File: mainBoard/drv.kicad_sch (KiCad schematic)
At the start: 6 parts

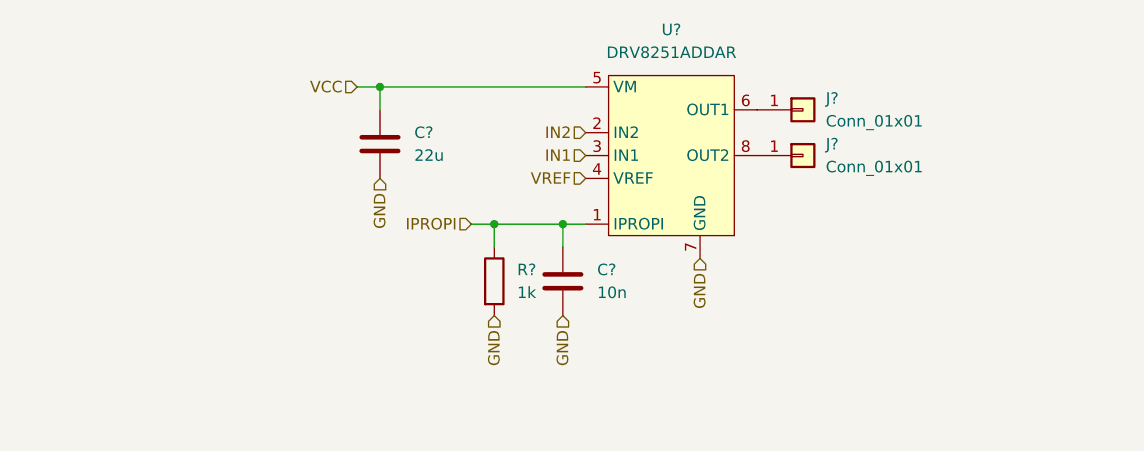
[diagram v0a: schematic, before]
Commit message: LEDky, měření napájení, připojení DRV atd.
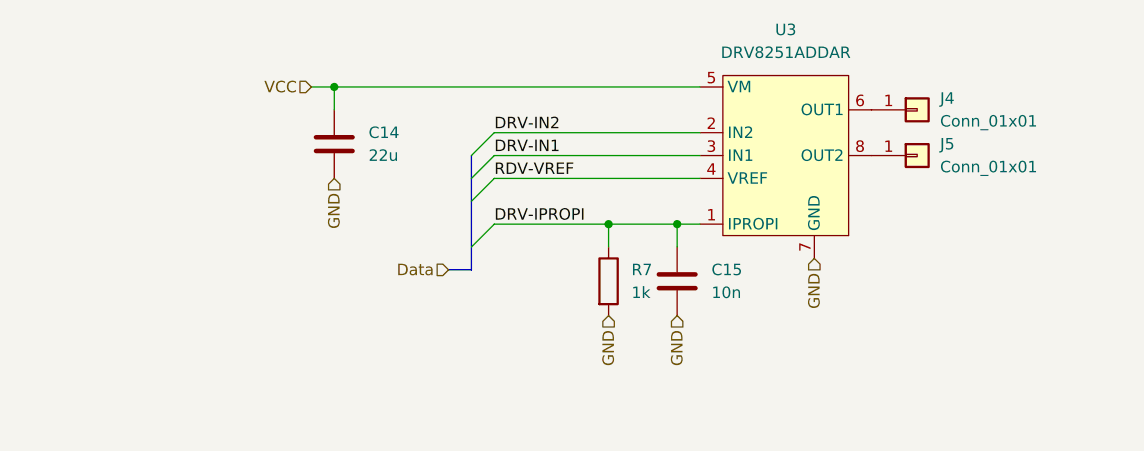
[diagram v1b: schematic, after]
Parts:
- gave numbers to parts that had none: 6
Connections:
- net IN1 renamed DRV-IN1
- net IN2 renamed DRV-IN2
- net IPROPI renamed DRV-IPROPI
- net VREF renamed RDV-VREF
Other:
- moved on the sheet: C14, C15, J4, J5, R7, U3

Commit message: Pouzdra
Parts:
- J4, J5: footprint (none) -> Connector_Pin:Pin_D1.0mm_L10.0mm
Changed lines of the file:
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@@
       (effects (font (size 1.27 1.27)) (justify left))
     )
-    (property "Footprint" "" (at 179.07 78.74 0)
+    (property "Footprint" "Connector_Pin:Pin_D1.0mm_L10.0mm" (at 179.07 78.74 0)
       (effects (font (size 1.27 1.27)) hide)
     )
@@
       (effects (font (size 1.27 1.27)) (justify left))
     )
-    (property "Footprint" "" (at 179.07 83.82 0)
+    (property "Footprint" "Connector_Pin:Pin_D1.0mm_L10.0mm" (at 179.07 83.82 0)
       (effects (font (size 1.27 1.27)) hide)
     )

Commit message: test-pointy a zdvojení konektorů
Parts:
- added J8: Conn_01x02, Connector_Phoenix_MC:PhoenixContact_MCV_1,5_2-G-3.81_1x02_P3.81mm_Vertical, symbol Connector_Generic:Conn_01x02
- added TP1, TP2: Conn_01x01, Connector_Pin:Pin_D0.7mm_L6.5mm_W1.8mm_FlatFork, symbol Connector_Generic:Conn_01x01
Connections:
- net DRV-IPROPI: now also TP1.1 (Pin_1)
- net RDV-VREF: now also TP2.1 (Pin_1)
- net at J4.1 (Pin_1), U3.6 (OUT1): now also J8.2 (Pin_2)
- net at J5.1 (Pin_1), U3.8 (OUT2): now also J8.1 (Pin_1)
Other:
- moved on the sheet: C14, J4, J5

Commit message: WIP
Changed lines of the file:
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@@
   (junction (at 152.4 91.44) (diameter 0) (color 0 0 0 0)
   )
-  (bus_entry (at 114.3 88.9) (size 2.54 -2.54)
-    (stroke (width 0) (type default))
-  )
-  (bus_entry (at 114.3 86.36) (size 2.54 -2.54)
-    (stroke (width 0) (type default))
-  )
-  (bus_entry (at 114.3 93.98) (size 2.54 -2.54)
-    (stroke (width 0) (type default))
-  )
-  (bus_entry (at 114.3 83.82) (size 2.54 -2.54)
+  (bus_entry (at 116.84 86.36) (size -2.54 2.54)
+    (stroke (width 0) (type default))
+  )
+  (bus_entry (at 116.84 83.82) (size -2.54 2.54)
+    (stroke (width 0) (type default))
+  )
+  (bus_entry (at 116.84 81.28) (size -2.54 2.54)
+    (stroke (width 0) (type default))
+  )
+  (bus_entry (at 116.84 91.44) (size -2.54 2.54)
     (stroke (width 0) (type default))
   )
@@
     (stroke (width 0) (type default))
   )
+  (wire (pts (xy 144.78 91.44) (xy 144.78 93.98))
+    (stroke (width 0) (type default))
+  )
+  (wire (pts (xy 96.52 76.2) (xy 99.06 76.2))
+    (stroke (width 0) (type default))
+  )
+  (wire (pts (xy 139.7 91.44) (xy 144.78 91.44))
+    (stroke (width 0) (type default))
+  )
+  (wire (pts (xy 176.53 78.74) (xy 173.99 78.74))
+    (stroke (width 0) (type default))
+  )
+  (wire (pts (xy 179.07 88.9) (xy 179.07 83.82))
+    (stroke (width 0) (type default))
+  )
+  (wire (pts (xy 152.4 91.44) (xy 154.94 91.44))
+    (stroke (width 0) (type default))
+  )
+  (wire (pts (xy 132.08 86.36) (xy 132.08 93.98))
+    (stroke (width 0) (type default))
+  )
+  (wire (pts (xy 181.61 83.82) (xy 179.07 83.82))
+    (stroke (width 0) (type default))
+  )
+  (wire (pts (xy 116.84 91.44) (xy 139.7 91.44))
+    (stroke (width 0) (type default))
+  )
+  (wire (pts (xy 181.61 88.9) (xy 179.07 88.9))
+    (stroke (width 0) (type default))
+  )
+  (wire (pts (xy 116.84 81.28) (xy 154.94 81.28))
+    (stroke (width 0) (type default))
+  )
+  (bus (pts (xy 111.76 96.52) (xy 114.3 96.52))
+    (stroke (width 0) (type default))
+  )
+  (wire (pts (xy 152.4 91.44) (xy 152.4 93.98))
+    (stroke (width 0) (type default))
+  )
+  (wire (pts (xy 116.84 83.82) (xy 154.94 83.82))
+    (stroke (width 0) (type default))
+  )
   (bus (pts (xy 114.3 83.82) (xy 114.3 86.36))
     (stroke (width 0) (type default))
   )
-  (wire (pts (xy 144.78 91.44) (xy 144.78 93.98))
-    (stroke (width 0) (type default))
-  )
-  (wire (pts (xy 96.52 76.2) (xy 99.06 76.2))
-    (stroke (width 0) (type default))
-  )
-  (wire (pts (xy 139.7 91.44) (xy 144.78 91.44))
-    (stroke (width 0) (type default))
-  )
-  (wire (pts (xy 176.53 78.74) (xy 173.99 78.74))
-    (stroke (width 0) (type default))
-  )
-  (wire (pts (xy 179.07 88.9) (xy 179.07 83.82))
-    (stroke (width 0) (type default))
-  )
-  (wire (pts (xy 152.4 91.44) (xy 154.94 91.44))
-    (stroke (width 0) (type default))
-  )
-  (wire (pts (xy 132.08 86.36) (xy 132.08 93.98))
-    (stroke (width 0) (type default))
-  )
-  (wire (pts (xy 181.61 83.82) (xy 179.07 83.82))
-    (stroke (width 0) (type default))
-  )
-  (wire (pts (xy 116.84 91.44) (xy 139.7 91.44))
-    (stroke (width 0) (type default))
-  )
-  (wire (pts (xy 181.61 88.9) (xy 179.07 88.9))
-    (stroke (width 0) (type default))
-  )
-  (wire (pts (xy 116.84 81.28) (xy 154.94 81.28))
+  (wire (pts (xy 179.07 83.82) (xy 173.99 83.82))
     (stroke (width 0) (type default))
   )
@@
     (stroke (width 0) (type default))
   )
-  (bus (pts (xy 111.76 96.52) (xy 114.3 96.52))
-    (stroke (width 0) (type default))
-  )
-  (wire (pts (xy 152.4 91.44) (xy 152.4 93.98))
-    (stroke (width 0) (type default))
-  )
-  (wire (pts (xy 116.84 83.82) (xy 154.94 83.82))
+  (wire (pts (xy 132.08 86.36) (xy 154.94 86.36))
+    (stroke (width 0) (type default))
+  )
+  (wire (pts (xy 116.84 86.36) (xy 132.08 86.36))
+    (stroke (width 0) (type default))
+  )
+  (wire (pts (xy 181.61 78.74) (xy 176.53 78.74))
+    (stroke (width 0) (type default))
+  )
+  (wire (pts (xy 176.53 91.44) (xy 176.53 78.74))
+    (stroke (width 0) (type default))
+  )
+  (wire (pts (xy 181.61 91.44) (xy 176.53 91.44))
+    (stroke (width 0) (type default))
+  )
+  (wire (pts (xy 99.06 76.2) (xy 99.06 78.74))
+    (stroke (width 0) (type default))
+  )
+  (wire (pts (xy 144.78 91.44) (xy 152.4 91.44))
     (stroke (width 0) (type default))
   )
   (bus (pts (xy 114.3 86.36) (xy 114.3 88.9))
-    (stroke (width 0) (type default))
-  )
-  (wire (pts (xy 179.07 83.82) (xy 173.99 83.82))
-    (stroke (width 0) (type default))
-  )
-  (wire (pts (xy 132.08 86.36) (xy 154.94 86.36))
-    (stroke (width 0) (type default))
-  )
-  (wire (pts (xy 181.61 78.74) (xy 176.53 78.74))
-    (stroke (width 0) (type default))
-  )
-  (wire (pts (xy 176.53 91.44) (xy 176.53 78.74))
-    (stroke (width 0) (type default))
-  )
-  (wire (pts (xy 181.61 91.44) (xy 176.53 91.44))
-    (stroke (width 0) (type default))
-  )
-  (wire (pts (xy 116.84 86.36) (xy 132.08 86.36))
-    (stroke (width 0) (type default))
-  )
-  (wire (pts (xy 99.06 76.2) (xy 99.06 78.74))
-    (stroke (width 0) (type default))
-  )
-  (wire (pts (xy 144.78 91.44) (xy 152.4 91.44))
     (stroke (width 0) (type default))
   )
@@
     (effects (font (size 1.27 1.27)) (justify right))
   )
-  (hierarchical_label "Data" (shape input) (at 111.76 96.52 180) (fields_autoplaced)
+  (hierarchical_label "Data" (shape bidirectional) (at 111.76 96.52 180) (fields_autoplaced)
     (effects (font (size 1.27 1.27)) (justify right))
   )
@@
       (effects (font (size 1.27 1.27)) hide)
     )
+    (pin "1")
     (pin "2")
-    (pin "1")
-    (instances
-      (project "mainBoard"
+    (instances
+      (project "mainBoard"

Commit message: ERC
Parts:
- removed U3: DRV8251ADDAR, Package_SO:SOIC-8-1EP_3.9x4.9mm_P1.27mm_EP2.62x3.51mm_ThermalVias, symbol Robotarna_KiCad_Library:DRV8251ADDAR
- added U4: DRV8251ADDAR, Package_SO:SOIC-8-1EP_3.9x4.9mm_P1.27mm_EP2.62x3.51mm_ThermalVias, symbol RKL-MotorDrivers:DRV8251ADDAR
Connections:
- net GND: now also U4.7 (GND), U4.9 (GND)
- net VCC: now also U4.5 (VM)
- net at J4.1 (Pin_1), J8.2 (Pin_2): now also U4.6 (OUT1)
- net at J5.1 (Pin_1), J8.1 (Pin_1): now also U4.8 (OUT2)
- net DRV-IPROPI renamed Data.PROUD
- net Data.PROUD: now also U4.1 (IPROPI)
- net RDV-VREF renamed Data.VREF
- net Data.VREF: now also U4.4 (VREF)
- new net Data.IN1: U4.3 (IN1)
- new net Data.IN2: U4.2 (IN2)
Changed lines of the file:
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@@
   (junction (at 152.4 91.44) (diameter 0) (color 0 0 0 0)
   )
-  (bus_entry (at 116.84 86.36) (size -2.54 2.54)
-    (stroke (width 0) (type default))
-  )
-  (bus_entry (at 116.84 83.82) (size -2.54 2.54)
-    (stroke (width 0) (type default))
-  )
-  (bus_entry (at 116.84 81.28) (size -2.54 2.54)
-    (stroke (width 0) (type default))
-  )
-  (bus_entry (at 116.84 91.44) (size -2.54 2.54)
+  (bus_entry (at 114.3 83.82) (size 2.54 -2.54)
+    (stroke (width 0) (type default))
+  )
+  (bus_entry (at 114.3 86.36) (size 2.54 -2.54)
+    (stroke (width 0) (type default))
+  )
+  (bus_entry (at 114.3 93.98) (size 2.54 -2.54)
+    (stroke (width 0) (type default))
+  )
+  (bus_entry (at 114.3 88.9) (size 2.54 -2.54)
     (stroke (width 0) (type default))
   )
@@
     (stroke (width 0) (type default))
   )
+  (bus (pts (xy 114.3 93.98) (xy 114.3 96.52))
+    (stroke (width 0) (type default))
+  )
   (wire (pts (xy 144.78 91.44) (xy 144.78 93.98))
     (stroke (width 0) (type default))
@@
     (stroke (width 0) (type default))
   )
+  (wire (pts (xy 116.84 83.82) (xy 154.94 83.82))
+    (stroke (width 0) (type default))
+  )
+  (wire (pts (xy 181.61 88.9) (xy 179.07 88.9))
+    (stroke (width 0) (type default))
+  )
+  (bus (pts (xy 111.76 96.52) (xy 114.3 96.52))
+    (stroke (width 0) (type default))
+  )
+  (wire (pts (xy 116.84 86.36) (xy 132.08 86.36))
+    (stroke (width 0) (type default))
+  )
+  (wire (pts (xy 152.4 91.44) (xy 152.4 93.98))
+    (stroke (width 0) (type default))
+  )
+  (bus (pts (xy 114.3 83.82) (xy 114.3 86.36))
+    (stroke (width 0) (type default))
+  )
+  (wire (pts (xy 179.07 83.82) (xy 173.99 83.82))
+    (stroke (width 0) (type default))
+  )
+  (wire (pts (xy 132.08 86.36) (xy 154.94 86.36))
+    (stroke (width 0) (type default))
+  )
+  (wire (pts (xy 116.84 81.28) (xy 154.94 81.28))
+    (stroke (width 0) (type default))
+  )
   (wire (pts (xy 116.84 91.44) (xy 139.7 91.44))
     (stroke (width 0) (type default))
   )
-  (wire (pts (xy 181.61 88.9) (xy 179.07 88.9))
-    (stroke (width 0) (type default))
-  )
-  (wire (pts (xy 116.84 81.28) (xy 154.94 81.28))
-    (stroke (width 0) (type default))
-  )
-  (bus (pts (xy 111.76 96.52) (xy 114.3 96.52))
-    (stroke (width 0) (type default))
-  )
-  (wire (pts (xy 152.4 91.44) (xy 152.4 93.98))
-    (stroke (width 0) (type default))
-  )
-  (wire (pts (xy 116.84 83.82) (xy 154.94 83.82))
-    (stroke (width 0) (type default))
-  )
-  (bus (pts (xy 114.3 83.82) (xy 114.3 86.36))
-    (stroke (width 0) (type default))
-  )
-  (wire (pts (xy 179.07 83.82) (xy 173.99 83.82))
-    (stroke (width 0) (type default))
-  )
-  (bus (pts (xy 114.3 93.98) (xy 114.3 96.52))
-    (stroke (width 0) (type default))
-  )
-  (wire (pts (xy 132.08 86.36) (xy 154.94 86.36))
-    (stroke (width 0) (type default))
-  )
-  (wire (pts (xy 116.84 86.36) (xy 132.08 86.36))
-    (stroke (width 0) (type default))
-  )
   (wire (pts (xy 181.61 78.74) (xy 176.53 78.74))
     (stroke (width 0) (type default))
@@
     (stroke (width 0) (type default))
   )
-  (label "DRV-IN1" (at 116.84 83.82 0) (fields_autoplaced)
+  (label "Data.IN2" (at 116.84 81.28 0)
     (effects (font (size 1.27 1.27)) (justify left bottom))
   )
-  (label "DRV-IPROPI" (at 116.84 91.44 0) (fields_autoplaced)
+  (label "Data.VREF" (at 116.84 86.36 0)
     (effects (font (size 1.27 1.27)) (justify left bottom))
   )
-  (label "DRV-IN2" (at 116.84 81.28 0) (fields_autoplaced)
+  (label "Data.PROUD" (at 116.84 91.44 0)
     (effects (font (size 1.27 1.27)) (justify left bottom))
   )
-  (label "RDV-VREF" (at 116.84 86.36 0) (fields_autoplaced)
+  (label "Data.IN1" (at 116.84 83.82 0)
     (effects (font (size 1.27 1.27)) (justify left bottom))
   )
@@
     (effects (font (size 1.27 1.27)) (justify right))
   )
-  (hierarchical_label "Data" (shape bidirectional) (at 111.76 96.52 180) (fields_autoplaced)
+  (hierarchical_label "Data{IN1 IN2 VREF PROUD}" (shape bidirectional) (at 111.76 96.52 180) (fields_autoplaced)
     (effects (font (size 1.27 1.27)) (justify right))
   )
@@
     )
   )
-  (symbol (lib_id "Robotarna_KiCad_Library:DRV8251ADDAR") (at 165.1 76.2 0) (unit 1)
-    (in_bom yes) (on_board yes) (dnp no) (fields_autoplaced)
-    (property "Reference" "U3" (at 164.465 69.85 0)
+  (symbol (lib_id "RKL-MotorDrivers:DRV8251ADDAR") (at 165.1 76.2 0) (unit 1)
+    (in_bom yes) (on_board yes) (dnp no) (fields_autoplaced)
+    (property "Reference" "U4" (at 164.465 69.85 0)
       (effects (font (size 1.27 1.27)))
     )
@@
       (project "mainBoard"
         (path "/30ed06d7-0b03-4878-b461-066cda7e7438/007b5876-baf1-4b85-a507-5fa12bfe2ac5"
-          (reference "U3") (unit 1)
-        )
-      )
+          (reference "U4") (unit 1)
+        )
+      )

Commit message: WIP
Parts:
- renumbered U4 to U3
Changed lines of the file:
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@@
   (symbol (lib_id "RKL-MotorDrivers:DRV8251ADDAR") (at 165.1 76.2 0) (unit 1)
     (in_bom yes) (on_board yes) (dnp no) (fields_autoplaced)
-    (property "Reference" "U4" (at 164.465 69.85 0)
+    (property "Reference" "U3" (at 164.465 69.85 0)
       (effects (font (size 1.27 1.27)))
     )
@@
       (project "mainBoard"
         (path "/30ed06d7-0b03-4878-b461-066cda7e7438/007b5876-baf1-4b85-a507-5fa12bfe2ac5"
-          (reference "U4") (unit 1)
+          (reference "U3") (unit 1)
         )
       )

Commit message: Popisky
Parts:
- renumbered J4 to M1, J5 to M2
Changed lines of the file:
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@@
     (stroke (width 0) (type default))
   )
-  (label "Data.IN2" (at 116.84 81.28 0)
+  (label "Data.IN2" (at 116.84 81.28 0) (fields_autoplaced)
     (effects (font (size 1.27 1.27)) (justify left bottom))
   )
-  (label "Data.VREF" (at 116.84 86.36 0)
+  (label "Data.VREF" (at 116.84 86.36 0) (fields_autoplaced)
     (effects (font (size 1.27 1.27)) (justify left bottom))
   )
-  (label "Data.PROUD" (at 116.84 91.44 0)
+  (label "Data.PROUD" (at 116.84 91.44 0) (fields_autoplaced)
     (effects (font (size 1.27 1.27)) (justify left bottom))
   )
-  (label "Data.IN1" (at 116.84 83.82 0)
+  (label "Data.IN1" (at 116.84 83.82 0) (fields_autoplaced)
     (effects (font (size 1.27 1.27)) (justify left bottom))
   )
@@
   (symbol (lib_id "Connector_Generic:Conn_01x01") (at 186.69 78.74 0) (unit 1)
     (in_bom yes) (on_board yes) (dnp no) (fields_autoplaced)
-    (property "Reference" "J4" (at 189.23 77.4699 0)
+    (property "Reference" "M1" (at 189.23 77.4699 0)
       (effects (font (size 1.27 1.27)) (justify left))
     )
@@
       (project "mainBoard"
         (path "/30ed06d7-0b03-4878-b461-066cda7e7438/007b5876-baf1-4b85-a507-5fa12bfe2ac5"
-          (reference "J4") (unit 1)
+          (reference "M1") (unit 1)
         )
       )
@@
   (symbol (lib_id "Connector_Generic:Conn_01x01") (at 186.69 83.82 0) (unit 1)
     (in_bom yes) (on_board yes) (dnp no) (fields_autoplaced)
-    (property "Reference" "J5" (at 189.23 82.5499 0)
+    (property "Reference" "M2" (at 189.23 82.5499 0)
       (effects (font (size 1.27 1.27)) (justify left))
     )
@@
       (project "mainBoard"
         (path "/30ed06d7-0b03-4878-b461-066cda7e7438/007b5876-baf1-4b85-a507-5fa12bfe2ac5"
-          (reference "J5") (unit 1)
+          (reference "M2") (unit 1)
         )
       )
